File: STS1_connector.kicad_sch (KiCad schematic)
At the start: 2 parts

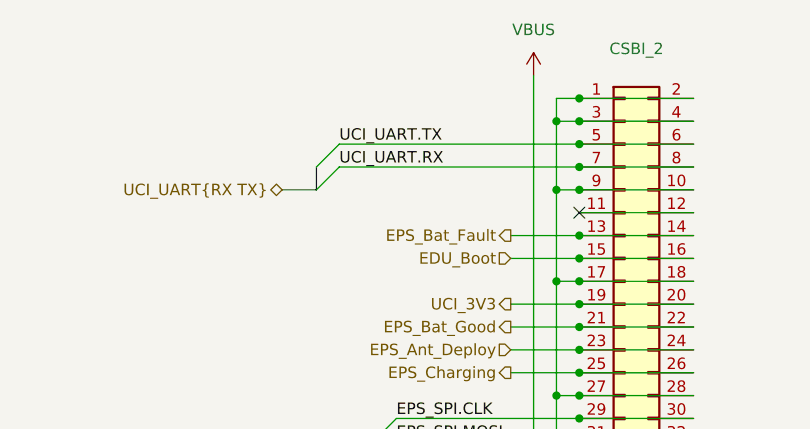
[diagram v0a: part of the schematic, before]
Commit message: feat: layout changed for new RF part
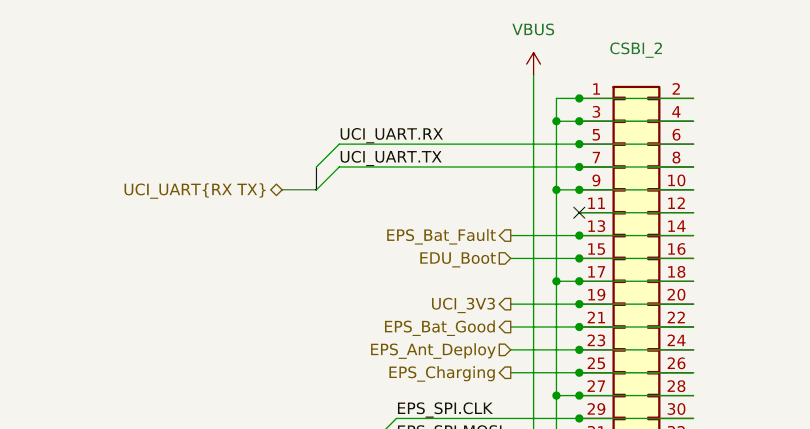
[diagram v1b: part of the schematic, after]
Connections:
- net UCI_UART.RX: now also CSBI_2.5 (Pin_5), CSBI_2.6 (Pin_6); no longer CSBI_2.7 (Pin_7), CSBI_2.8 (Pin_8)
- net UCI_UART.TX: now also CSBI_2.7 (Pin_7), CSBI_2.8 (Pin_8); no longer CSBI_2.5 (Pin_5), CSBI_2.6 (Pin_6)
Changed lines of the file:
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@@
     (effects (font (size 1.27 1.27)) (justify left bottom))
   )
-  (label "UCI_UART.RX" (at 147.32 53.34 0)
+  (label "UCI_UART.TX" (at 147.32 53.34 0)
     (effects (font (size 1.27 1.27)) (justify left bottom))
   )
@@
     (effects (font (size 1.27 1.27)) (justify left bottom))
   )
-  (label "UCI_UART.TX" (at 147.32 50.8 0)
+  (label "UCI_UART.RX" (at 147.32 50.8 0)
     (effects (font (size 1.27 1.27)) (justify left bottom))
   )

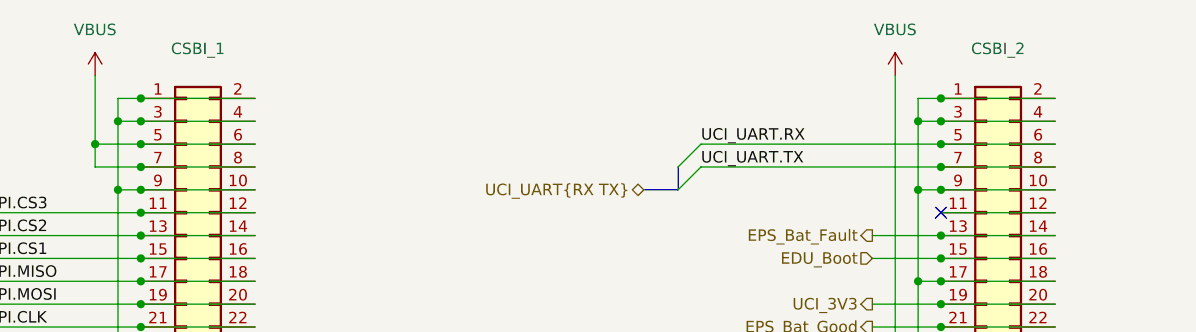
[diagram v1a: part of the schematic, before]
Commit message: Fix footprint assignments: all CSBI headers should have J designator
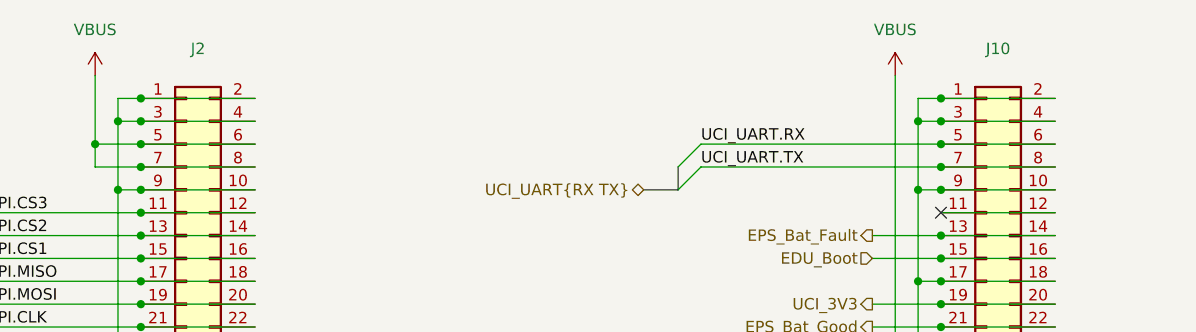
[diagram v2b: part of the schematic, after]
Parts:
- renumbered CSBI_2 to J10, CSBI_1 to J2
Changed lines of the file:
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@@
   (symbol (lib_id "Connector_Generic:Conn_02x25_Odd_Even") (at 90.17 76.2 0) (unit 1)
     (in_bom yes) (on_board yes)
-    (property "Reference" "CSBI_1" (id 0) (at 91.44 40.2082 0))
+    (property "Reference" "J2" (id 0) (at 91.44 40.2082 0))
     (property "Value" "~" (id 1) (at 91.44 42.5196 0))
     (property "Footprint" "Connector_PinSocket_2.00mm:PinSocket_2x25_P2.00mm_Vertical" (id 2) (at 90.17 76.2 0)
@@
   (symbol (lib_id "Connector_Generic:Conn_02x25_Odd_Even") (at 179.07 76.2 0) (unit 1)
     (in_bom yes) (on_board yes)
-    (property "Reference" "CSBI_2" (id 0) (at 180.34 40.2082 0))
+    (property "Reference" "J10" (id 0) (at 180.34 40.2082 0))
     (property "Value" "~" (id 1) (at 180.34 42.5196 0))
     (property "Footprint" "Connector_PinSocket_2.00mm:PinSocket_2x25_P2.00mm_Vertical" (id 2) (at 179.07 76.2 0)
